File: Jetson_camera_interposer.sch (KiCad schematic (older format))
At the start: 19 parts, among them J1 QSH-060-01-L-D-A, J2 QTH-060-01-L-D-A, J21 Conn_01x01, J22 Conn_01x01, J23 Conn_01x01, J24 Conn_01x01, J25 Conn_01x01, J26 Conn_01x01, J3 Conn_01x01, J4 Conn_01x01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

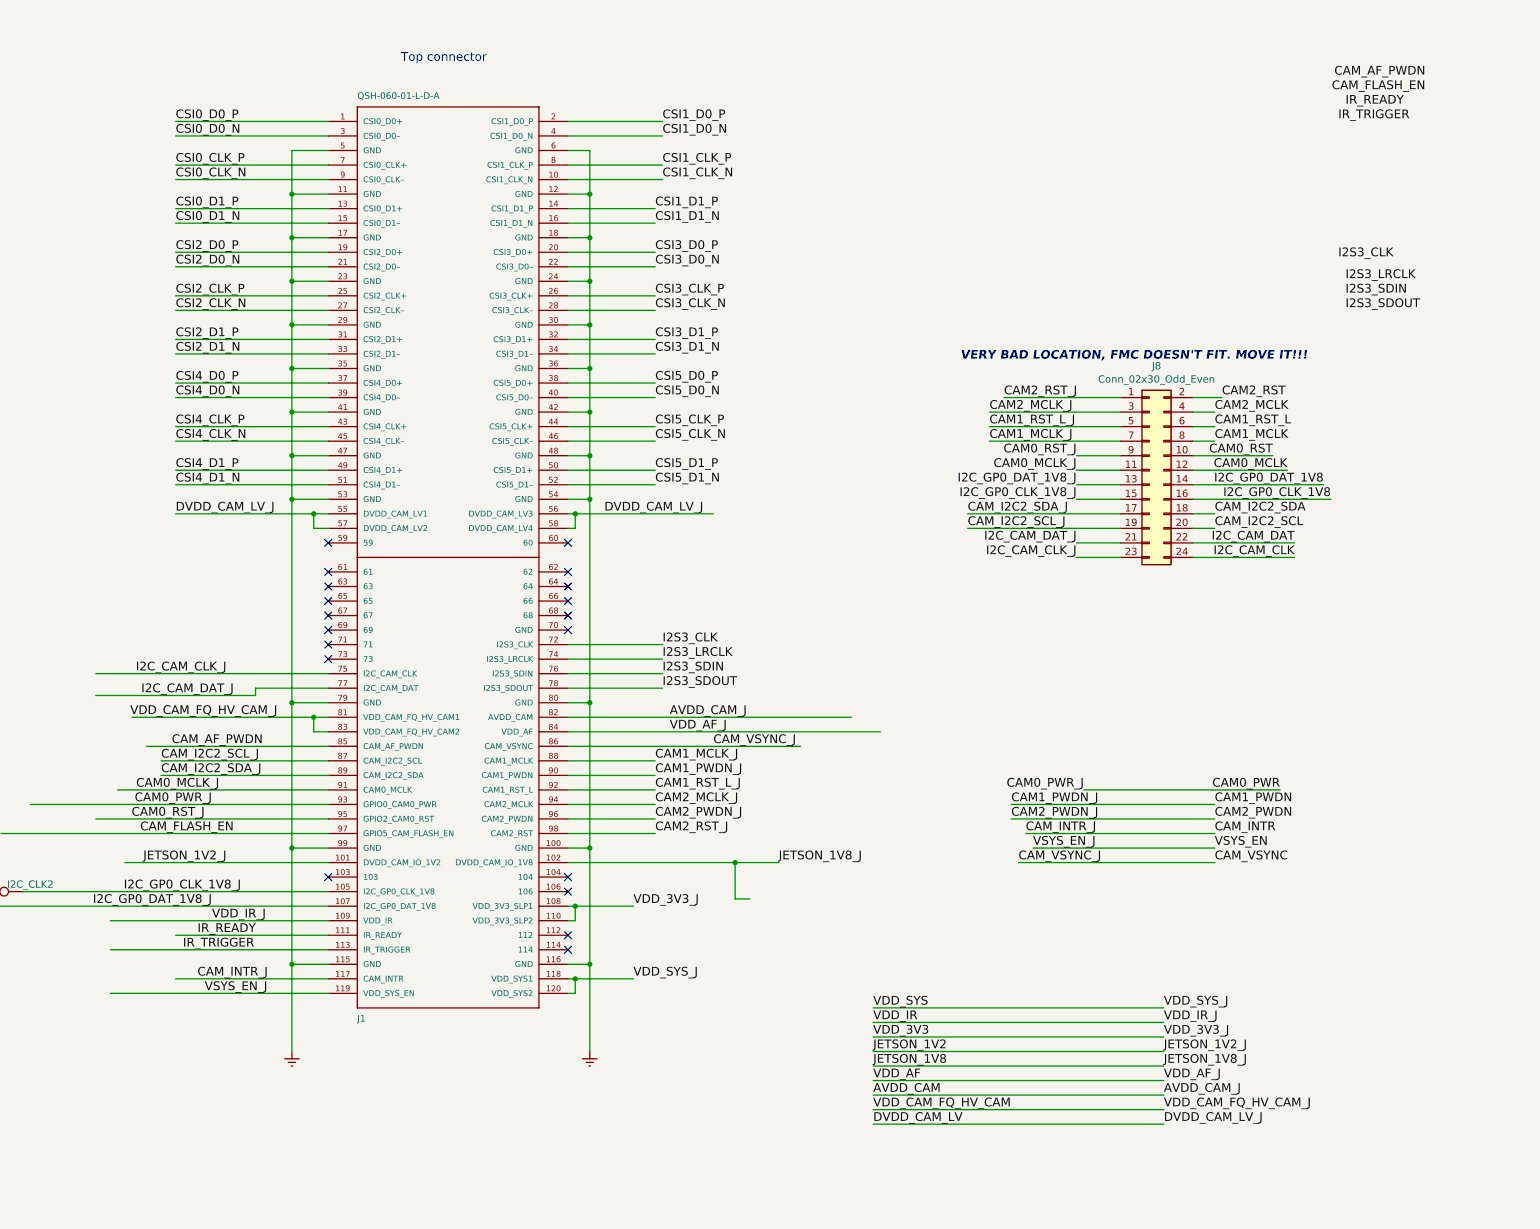
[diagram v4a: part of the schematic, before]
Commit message: leaving only single connector
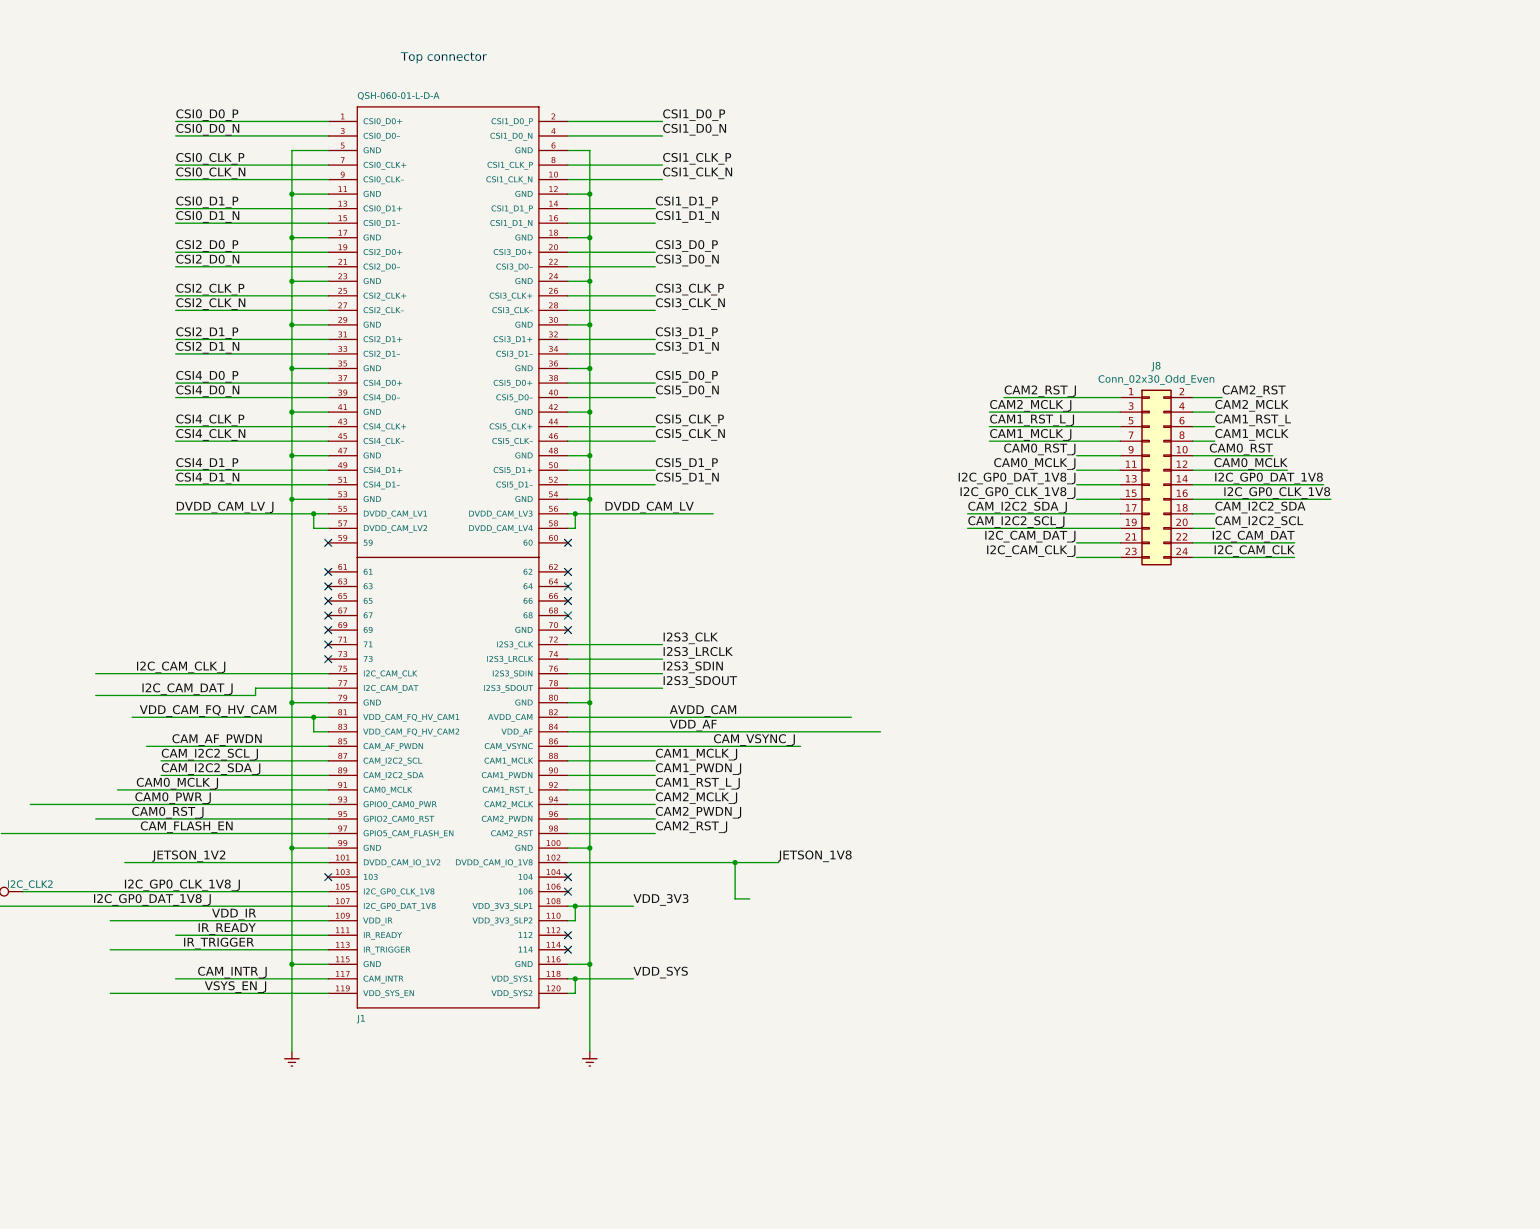
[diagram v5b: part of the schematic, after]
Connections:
- net labels removed: AVDD_CAM_J, JETSON_1V2_J, JETSON_1V8_J, VDD_3V3_J, VDD_AF_J, VDD_CAM_FQ_HV_CAM_J, VDD_IR_J, VDD_SYS_J
- wire segments 348 -> 333
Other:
- note removed: "VERY BAD LOCATION, FMC DOESN'T FIT. MOVE IT!!!"
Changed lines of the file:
@@
 NoConn ~ 8100 5400
 NoConn ~ 8100 5500
-Text Label 7400 5600 2    60   ~ 0
-I2C_CAM_CLK_J
-Text Label 7450 5750 2    60   ~ 0
-I2C_CAM_DAT_J
-Text Label 7350 6400 2    60   ~ 0
-CAM0_MCLK_J
-Text Label 7300 6500 2    60   ~ 0
-CAM0_PWR_J
 Text Label 7250 6600 2    60   ~ 0
 CAM0_RST_J
@@
 CAM_FLASH_EN
 Text Label 7400 6900 2    60   ~ 0
-JETSON_1V2_J
+JETSON_1V2
 Text Label 7500 7100 2    60   ~ 0
 I2C_GP0_CLK_1V8_J
@@
 CAM_VSYNC_J
 Text Label 11200 6900 0    60   ~ 0
-JETSON_1V8_J
+JETSON_1V8
 NoConn ~ 9750 4700
 NoConn ~ 9750 4900
@@
 NoConn ~ 9750 5200
 NoConn ~ 9750 5300
-Text Label 7050 4500 0    60   ~ 0
-DVDD_CAM_LV_J
-Text Label 10000 4500 0    60   ~ 0
-DVDD_CAM_LV_J
 Text Label 4450 4500 0    60   ~ 0
 DVDD_CAM_LV
@@
 VDD_SYS
 Text Label 10200 7700 0    60   ~ 0
-VDD_SYS_J
+VDD_SYS
 Text Label 4450 7200 0    60   ~ 0
 VDD_3V3
 Text Label 10200 7200 0    60   ~ 0
-VDD_3V3_J
+VDD_3V3
 Text Label 10450 5900 0    60   ~ 0
-AVDD_CAM_J
+AVDD_CAM
 Text Label 10450 6000 0    60   ~ 0
-VDD_AF_J
+VDD_AF
 Text Label 4500 5900 0    60   ~ 0
 AVDD_CAM
@@
 Text Label 1300 5900 0    60   ~ 0
 VDD_CAM_FQ_HV_CAM
-Text Label 7750 5900 2    60   ~ 0
-VDD_CAM_FQ_HV_CAM_J
 Text Label 7300 7300 0    60   ~ 0
-VDD_IR_J
+VDD_IR
 Text Label 7200 7400 0    60   ~ 0
 IR_READY
@@
 Wire Wire Line
 	8100 6300 6950 6300
-Text Label 6950 6200 0    60   ~ 0
-CAM_I2C2_SCL_J
-Text Label 6950 6300 0    60   ~ 0
-CAM_I2C2_SDA_J
 Wire Wire Line
 	2500 6200 950  6200
@@
 Text Label 4750 5700 0    60   ~ 0
 I2S3_SDOUT
-Text Label 13850 7900 0    60   ~ 0
-VDD_SYS_J
-Text Label 13850 8000 0    60   ~ 0
-VDD_IR_J
-Text Label 11850 8100 0    60   ~ 0
-VDD_3V3
-Text Label 11850 8200 0    60   ~ 0
-JETSON_1V2
-Text Label 11850 8300 0    60   ~ 0
-JETSON_1V8
-Text Label 11850 8400 0    60   ~ 0
-VDD_AF
-Text Label 11850 8500 0    60   ~ 0
-AVDD_CAM
-Text Label 11850 8600 0    60   ~ 0
-VDD_CAM_FQ_HV_CAM
-Text Label 11850 8700 0    60   ~ 0
-DVDD_CAM_LV
-Text Label 11850 7900 0    60   ~ 0
-VDD_SYS
-Text Label 11850 8000 0    60   ~ 0
-VDD_IR
-Text Label 13850 8100 0    60   ~ 0
-VDD_3V3_J
-Text Label 13850 8200 0    60   ~ 0
-JETSON_1V2_J
-Text Label 13850 8300 0    60   ~ 0
-JETSON_1V8_J
-Text Label 13850 8400 0    60   ~ 0
-VDD_AF_J
-Text Label 13850 8500 0    60   ~ 0
-AVDD_CAM_J
-Text Label 13850 8600 0    60   ~ 0
-VDD_CAM_FQ_HV_CAM_J
-Text Label 13850 8700 0    60   ~ 0
-DVDD_CAM_LV_J
 Wire Wire Line
 	9800 7200 10200 7200
@@
 Text Label 14750 4700 2    60   ~ 0
 I2C_CAM_DAT
-Text Label 15650 1500 2    60   ~ 0
-CAM_AF_PWDN
 Text Label 14700 4200 2    60   ~ 0
 CAM0_MCLK
-Text Label 15650 1600 2    60   ~ 0
-CAM_FLASH_EN
-Text Label 15100 1700 0    60   ~ 0
-IR_READY
-Text Label 15050 1800 0    60   ~ 0
-IR_TRIGGER
-Text Label 15050 2750 0    60   ~ 0
-I2S3_CLK
-Text Label 15100 2900 0    60   ~ 0
-I2S3_LRCLK
-Text Label 15100 3000 0    60   ~ 0
-I2S3_SDIN
-Text Label 15100 3100 0    60   ~ 0
-I2S3_SDOUT
 Text Label 14200 4000 0    60   ~ 0
 CAM1_MCLK
@@
 Text Label 4850 6100 2    60   ~ 0
 CAM_VSYNC
-Text Notes 12450 3450 0    60   Italic 12
-VERY BAD LOCATION, FMC DOESN'T FIT. MOVE IT!!!
-Text Label 12850 6900 0    60   ~ 0
-CAM_VSYNC_J
-Text Label 12950 6800 0    60   ~ 0
-VSYS_EN_J
-Text Label 12900 6700 0    60   ~ 0
-CAM_INTR_J
-Text Label 12800 6600 0    60   ~ 0
-CAM2_PWDN_J
-Text Label 12800 6500 0    60   ~ 0
-CAM1_PWDN_J
-Text Label 13300 6400 2    60   ~ 0
+Text Label 7300 6500 2    60   ~ 0
 CAM0_PWR_J
-Text Label 14200 6500 0    60   ~ 0
-CAM1_PWDN
-Text Label 14200 6600 0    60   ~ 0
-CAM2_PWDN
-Text Label 14200 6900 0    60   ~ 0
-CAM_VSYNC
-Text Label 14200 6800 0    60   ~ 0
-VSYS_EN
-Text Label 14200 6700 0    60   ~ 0
-CAM_INTR
-Text Label 14650 6400 2    60   ~ 0
-CAM0_PWR
-Wire Wire Line
-	11850 7900 13850 7900
-Wire Wire Line
-	11850 8000 13850 8000
-Wire Wire Line
-	11850 8100 13850 8100
-Wire Wire Line
-	11850 8200 13850 8200
-Wire Wire Line
-	11850 8300 13850 8300
-Wire Wire Line
-	11850 8400 13850 8400
-Wire Wire Line
-	11850 8500 13850 8500
-Wire Wire Line
-	11850 8600 13850 8600
-Wire Wire Line
-	11850 8700 13850 8700
-Wire Wire Line
-	13300 6400 14650 6400
-Wire Wire Line
-	12800 6500 14200 6500
-Wire Wire Line
-	12800 6600 14200 6600
-Wire Wire Line
-	12900 6700 14200 6700
-Wire Wire Line
-	12950 6800 14200 6800
-Wire Wire Line
-	12850 6900 14200 6900
+Text Label 7350 6400 2    60   ~ 0
+CAM0_MCLK_J
+Text Label 6950 6300 0    60   ~ 0
+CAM_I2C2_SDA_J
+Text Label 6950 6200 0    60   ~ 0
+CAM_I2C2_SCL_J
+Text Label 7750 5900 2    60   ~ 0
+VDD_CAM_FQ_HV_CAM
+Text Label 7450 5750 2    60   ~ 0
+I2C_CAM_DAT_J
+Text Label 7400 5600 2    60   ~ 0
+I2C_CAM_CLK_J
+Text Label 10000 4500 0    60   ~ 0
+DVDD_CAM_LV
+Text Label 7050 4500 0    60   ~ 0
+DVDD_CAM_LV_J
 $EndSCHEMATC

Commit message: continue routing
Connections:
- net labels removed: CAM_VSYNC_J, DVDD_CAM_LV_J
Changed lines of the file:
@@
 CAM0_PWR
 Text Label 1500 6600 2    60   ~ 0
-CAM0_RST_J
+CAM0_RST
 Text Label 1500 6700 2    60   ~ 0
 CAM_FLASH_EN
@@
 I2C_GP0_DAT_1V8_J
 Text Label 10750 6100 0    60   ~ 0
-CAM_VSYNC_J
+CAM_VSYNC
 Text Label 11200 6900 0    60   ~ 0
 JETSON_1V8
@@
 Text Label 7400 5600 2    60   ~ 0
 I2C_CAM_CLK_J
+Text Label 7050 4500 0    60   ~ 0
+DVDD_CAM_LV
 Text Label 10000 4500 0    60   ~ 0
 DVDD_CAM_LV
-Text Label 7050 4500 0    60   ~ 0
-DVDD_CAM_LV_J
 $EndSCHEMATC

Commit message: Done routing
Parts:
- removed GND1, GND2, GND3: TestP, TX2_Footprints:test_point, symbol TX2_Symbols:TEST_1P
- removed J21, J22, J23, J24, J25, J4, J5, J6: Conn_01x01, TX2_Footprints:ground_probe, symbol TX2_Symbols:Conn_01x01
- added J7: Conn_01x01, Pin_Headers:Pin_Header_Straight_1x1_Pitch2.54mm, symbol Connector_Generic:Conn_01x01
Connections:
- net labels removed: CAM_INTR_J, VSYS_EN_J
- wire segments 333 -> 308
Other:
- moved on the sheet: GND4, J26, J3

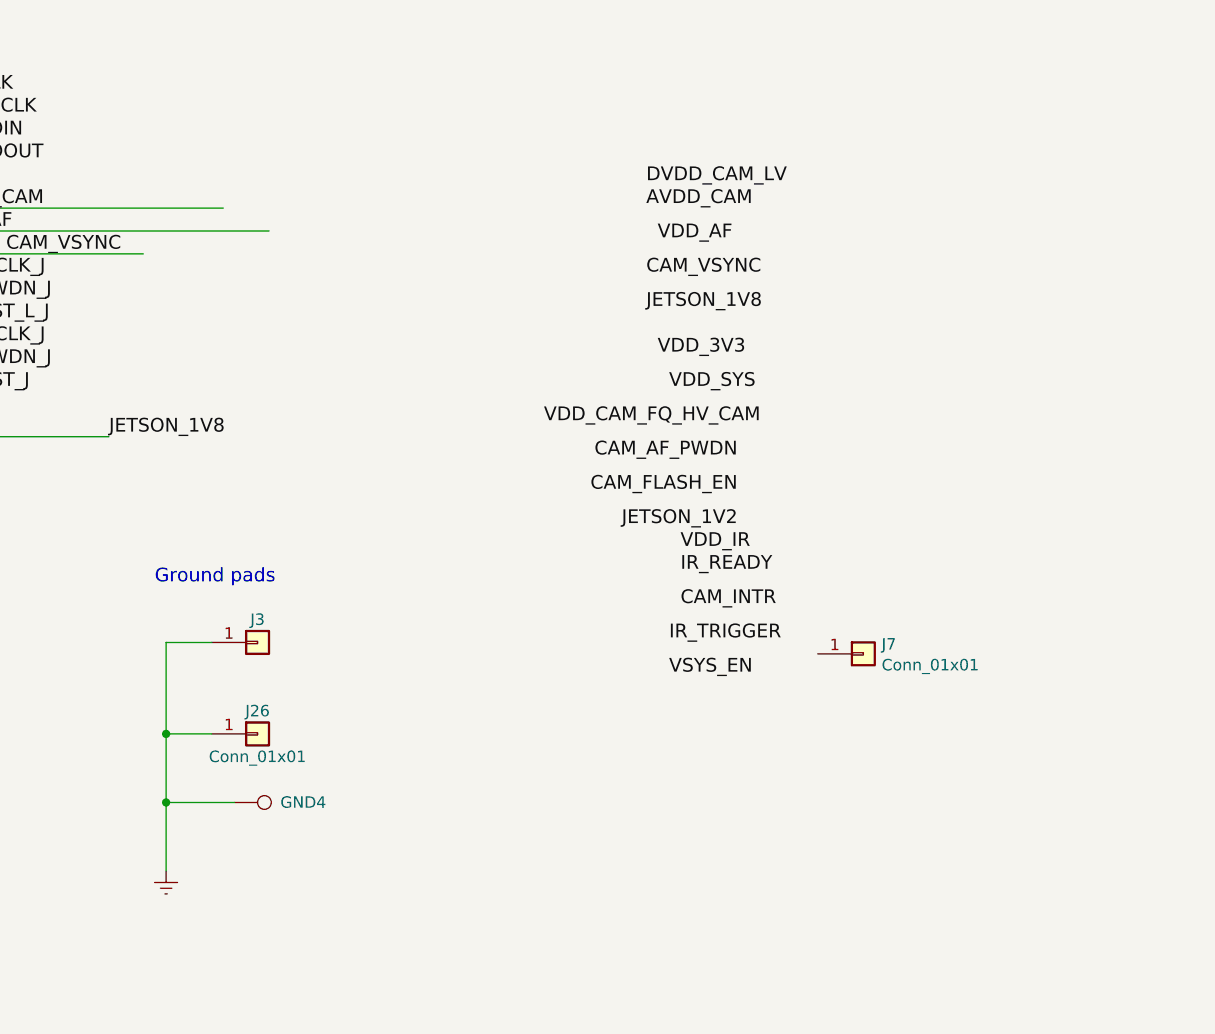
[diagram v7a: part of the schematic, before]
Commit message: Added debug pins to schematics
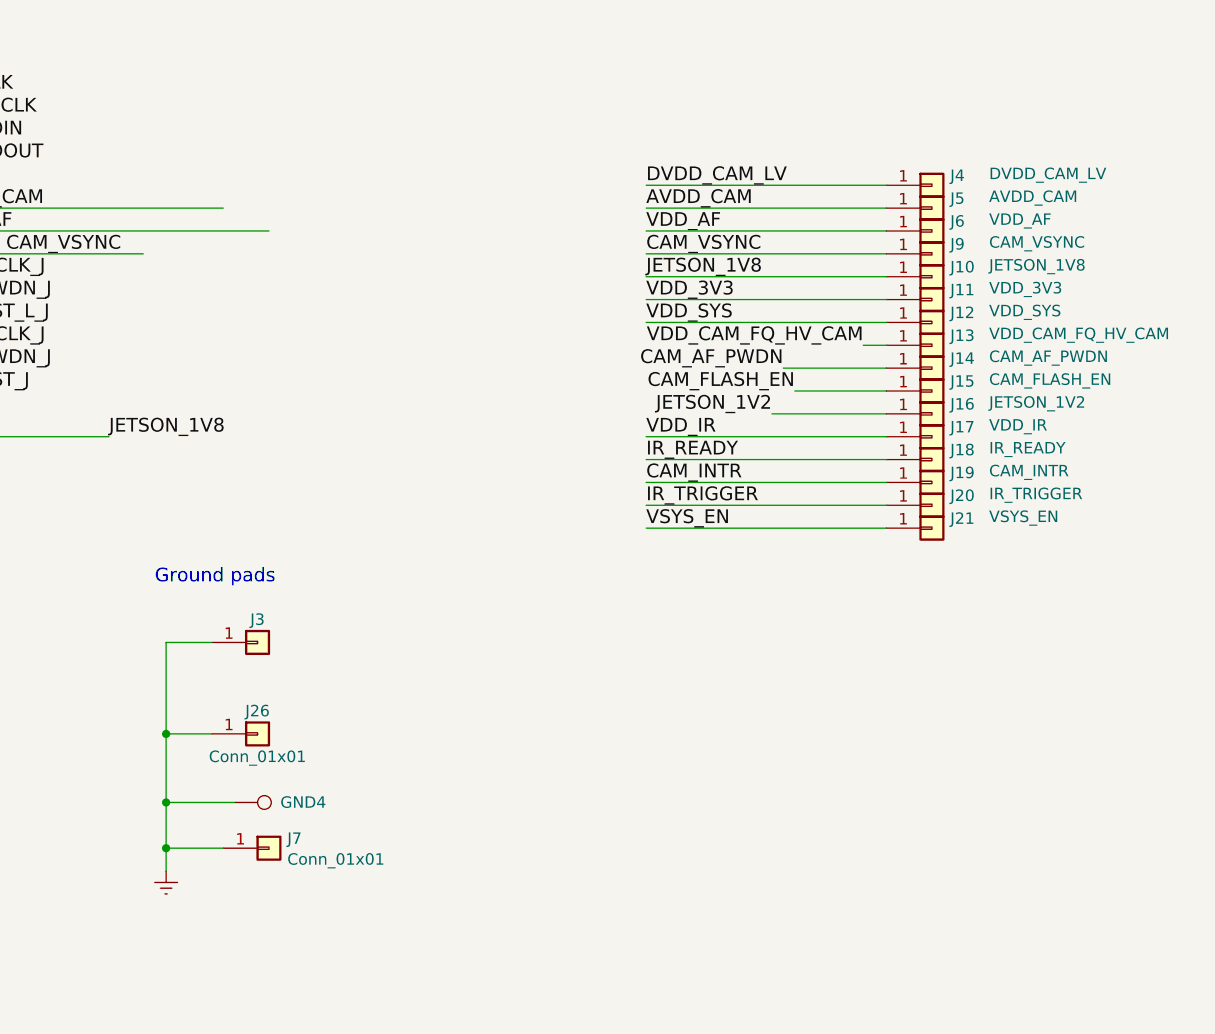
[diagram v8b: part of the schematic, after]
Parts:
- added J10: JETSON_1V8, Pin_Headers:Pin_Header_Straight_1x01_Pitch2.54mm, symbol Connector_Generic:Conn_01x01
- added J11: VDD_3V3, Pin_Headers:Pin_Header_Straight_1x01_Pitch2.54mm, symbol Connector_Generic:Conn_01x01
- added J12: VDD_SYS, Pin_Headers:Pin_Header_Straight_1x01_Pitch2.54mm, symbol Connector_Generic:Conn_01x01
- added J13: VDD_CAM_FQ_HV_CAM, Pin_Headers:Pin_Header_Straight_1x01_Pitch2.54mm, symbol Connector_Generic:Conn_01x01
- added J14: CAM_AF_PWDN, Pin_Headers:Pin_Header_Straight_1x01_Pitch2.54mm, symbol Connector_Generic:Conn_01x01
- added J15: CAM_FLASH_EN, Pin_Headers:Pin_Header_Straight_1x01_Pitch2.54mm, symbol Connector_Generic:Conn_01x01
- added J16: JETSON_1V2, Pin_Headers:Pin_Header_Straight_1x01_Pitch2.54mm, symbol Connector_Generic:Conn_01x01
- added J17: VDD_IR, Pin_Headers:Pin_Header_Straight_1x01_Pitch2.54mm, symbol Connector_Generic:Conn_01x01
- added J18: IR_READY, Pin_Headers:Pin_Header_Straight_1x01_Pitch2.54mm, symbol Connector_Generic:Conn_01x01
- added J19: CAM_INTR, Pin_Headers:Pin_Header_Straight_1x01_Pitch2.54mm, symbol Connector_Generic:Conn_01x01
- added J20: IR_TRIGGER, Pin_Headers:Pin_Header_Straight_1x01_Pitch2.54mm, symbol Connector_Generic:Conn_01x01
- added J21: VSYS_EN, Pin_Headers:Pin_Header_Straight_1x01_Pitch2.54mm, symbol Connector_Generic:Conn_01x01
- added J4: DVDD_CAM_LV, Pin_Headers:Pin_Header_Straight_1x01_Pitch2.54mm, symbol Connector_Generic:Conn_01x01
- added J5: AVDD_CAM, Pin_Headers:Pin_Header_Straight_1x01_Pitch2.54mm, symbol Connector_Generic:Conn_01x01
- added J6: VDD_AF, Pin_Headers:Pin_Header_Straight_1x01_Pitch2.54mm, symbol Connector_Generic:Conn_01x01
- added J9: CAM_VSYNC, Pin_Headers:Pin_Header_Straight_1x01_Pitch2.54mm, symbol Connector_Generic:Conn_01x01
- J7: footprint Pin_Headers:Pin_Header_Straight_1x1_Pitch2.54mm -> Pin_Headers:Pin_Header_Straight_1x01_Pitch2.54mm
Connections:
- wire segments 308 -> 326
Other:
- moved on the sheet: J7
